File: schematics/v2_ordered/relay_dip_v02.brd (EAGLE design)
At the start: 50 x 50 mm, 51 parts, among them IC1 74HCT04D, IC2 DS2432P

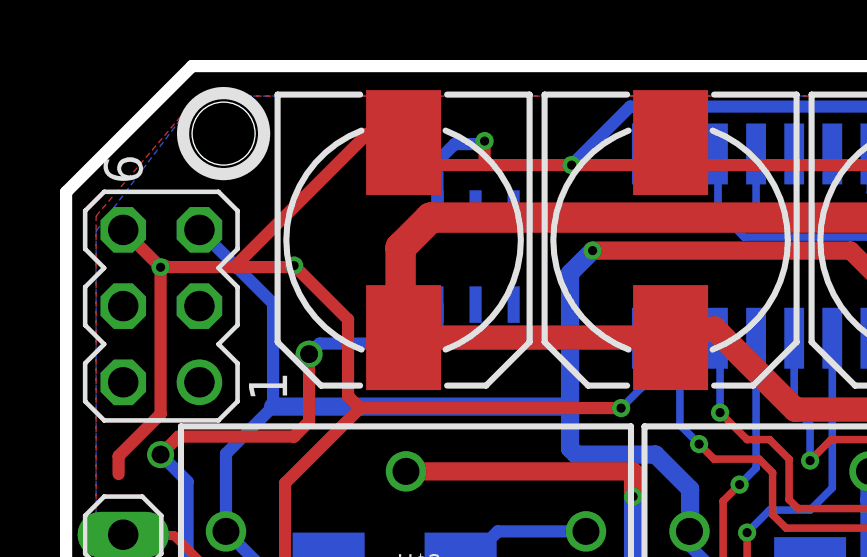
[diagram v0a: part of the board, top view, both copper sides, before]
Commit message: added v3, fixed ds2431 footprint, added quotation
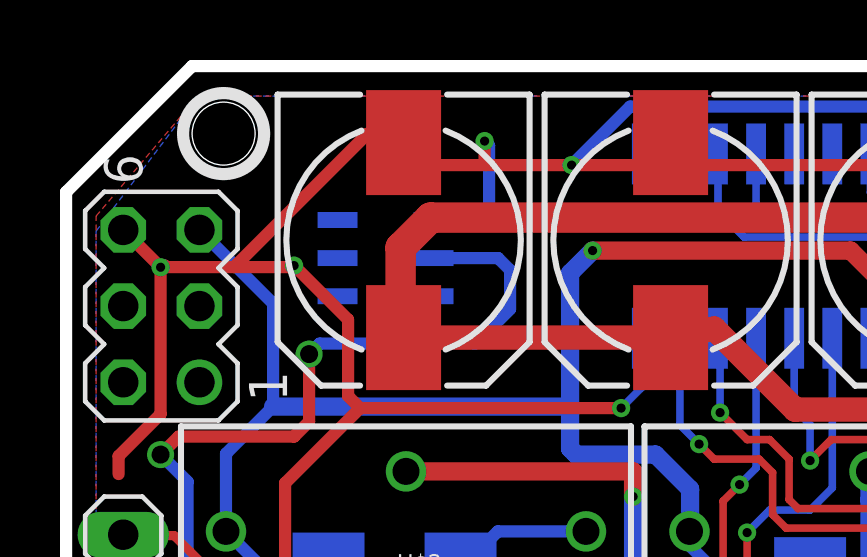
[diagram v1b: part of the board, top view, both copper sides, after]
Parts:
- removed IC2: DS2432P, 1wire:TSOC6
- added U1: DS2431P+T&R, JKW_CHIP:TSOC6
- D1, D2, D3, D4: value (none) -> ES2D
- JP1, JP2, JP3: value (none) -> 571-4-103321-5
- P1, P2, P3, P4: value (none) -> 696-SML-0805ICTR
- POW: value (none) -> 150080BS75000
- R1: value (none) -> 2.2k
- R10, R6, R8, R9: value 10k -> n.a. (10k)
- R2, R3, R4, R5: value 330R -> 200R
- R7: value 330R -> 120R
- S1: value SWITCH-MOMENTARY-2SMD -> n.a.
- SV3: value (none) -> 571-4-146262-1
- SV4: value (none) -> 649-68000-408HLF
- U$1, U$11, U$2, U$8: value RELAYPTH -> SRD-05VDC-SL-C
- U$12, U$3, U$7, U$9: value NMOSFET_SMD_223 -> DMN6068SE-13
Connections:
- new net N$6: IC1.12
- net 3V: now also IC1.13
- net GND: now also U1.1; no longer IC2.4
- net LD2: now also U1.2; no longer IC2.3
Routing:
- net LD2: track 30.2 -> 35.9 mm
- net GND: track 235.5 -> 236.6 mm
